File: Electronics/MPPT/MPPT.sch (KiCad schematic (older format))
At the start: 113 parts, among them J1 Solar Array, J2 Battery, J3 Car Power, J4 CAN_In, J5 CAN_Out, Q1 200N25N, Q2 200N25N, SW1 RESET, SW2 CAN Address, U1 PQMC3-D12-S9-S, U2 Nucleo_L432KC, U3 UCC37321, U4 INA210, U5 ADM3055E, U6 INA210, U7 CDSOT23-T24CAN

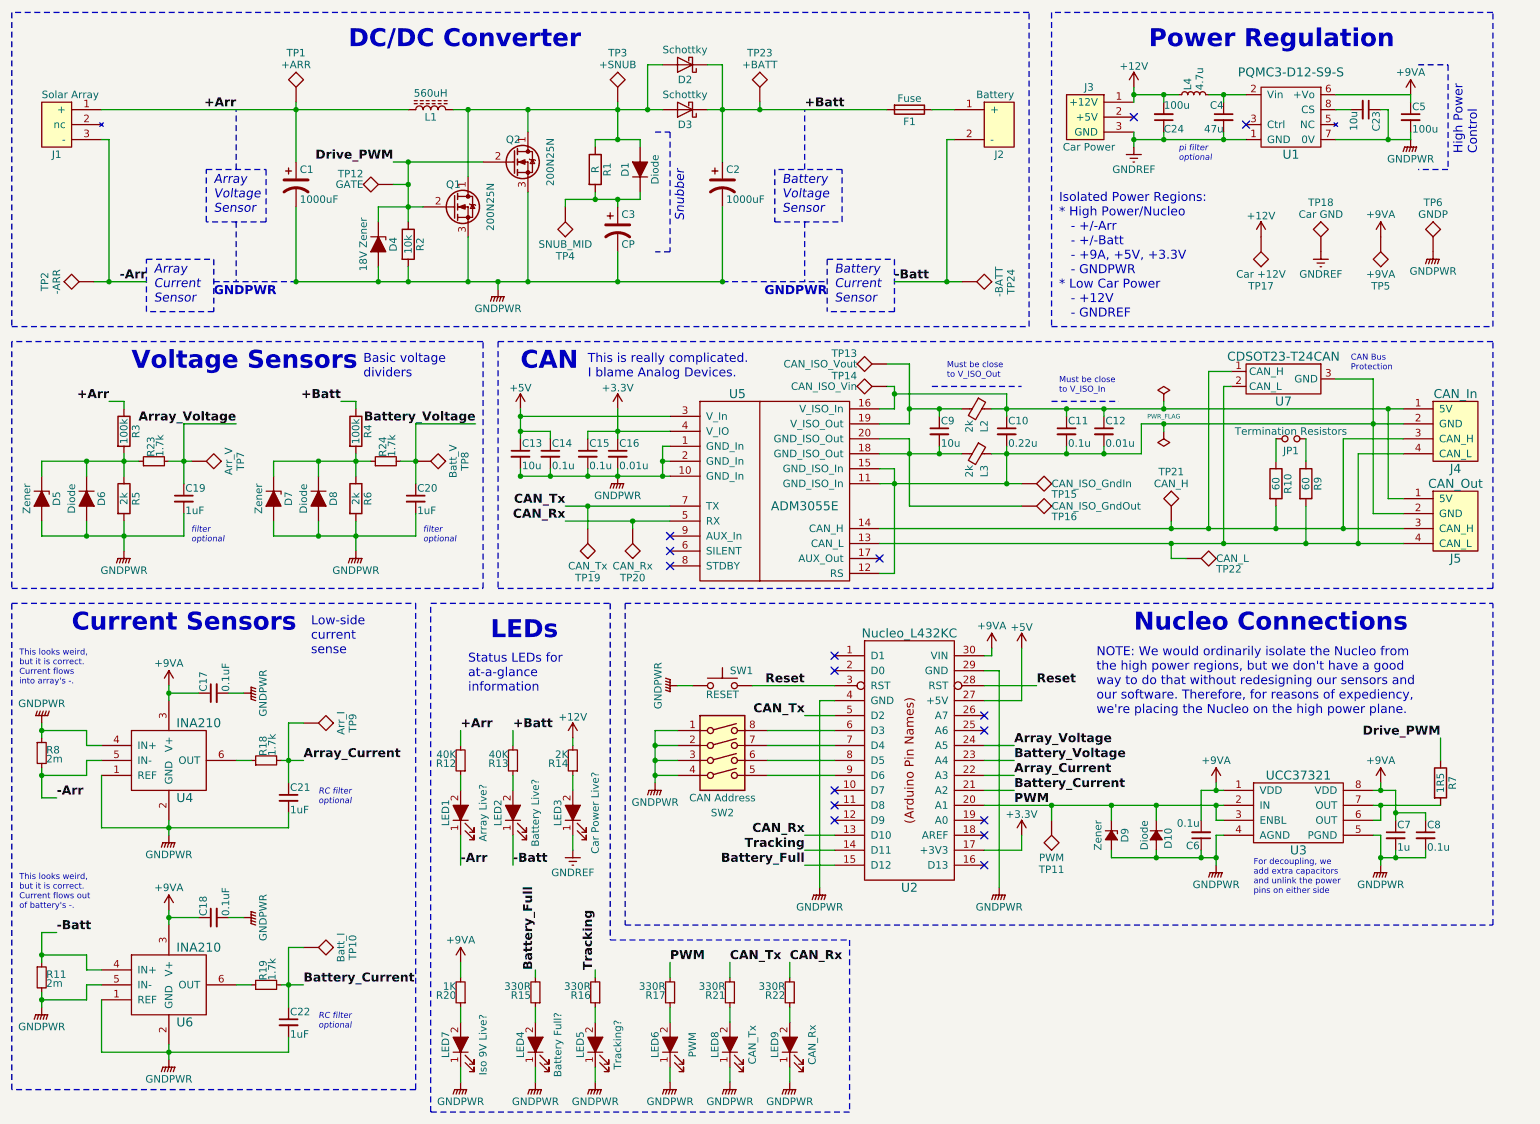
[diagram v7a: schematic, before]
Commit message: MPPT: Add Rslope to CAN chip on schematic.
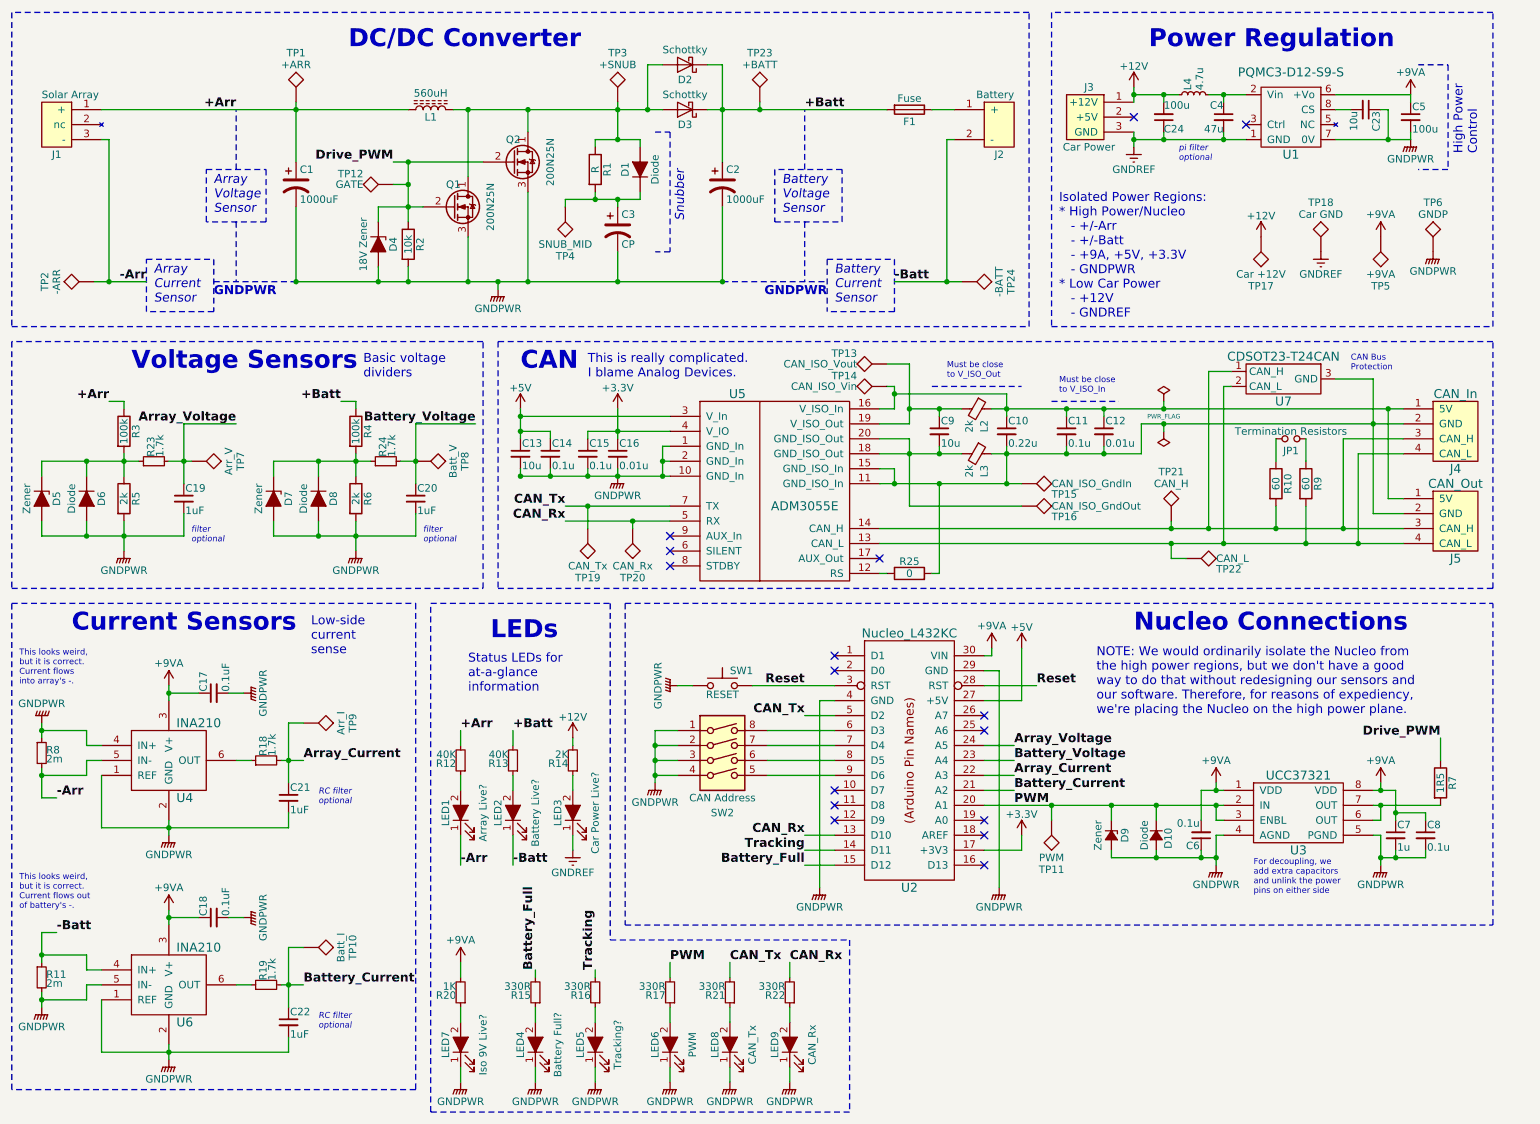
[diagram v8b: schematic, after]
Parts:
- added R25: 0, Resistors_SMD:R_0805, symbol R
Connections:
- net at C10.2, C11.2, C12.2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: now also R25.2; no longer U5.12 (RS)
- new net: R25.1, U5.12 (RS)
